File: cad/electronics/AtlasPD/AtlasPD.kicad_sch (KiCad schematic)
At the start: 0 parts

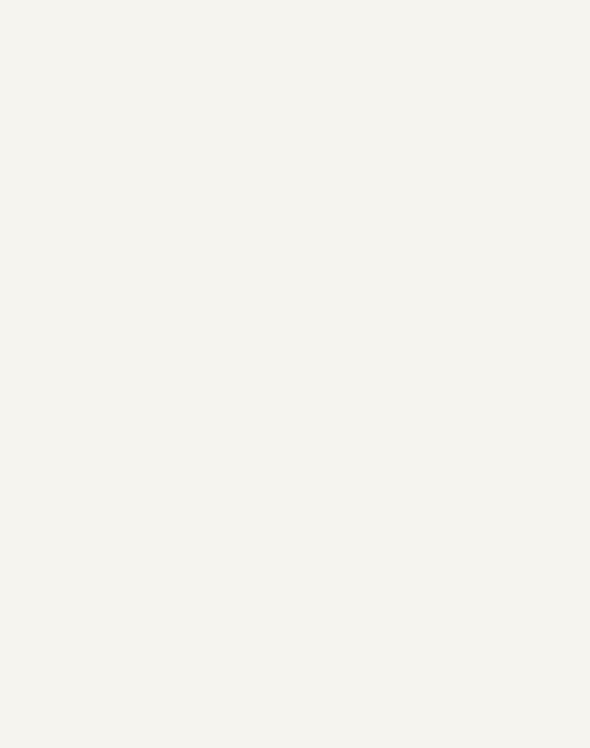
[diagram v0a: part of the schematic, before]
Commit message: Changing MCU design due to chip shortage affecting current design/plans
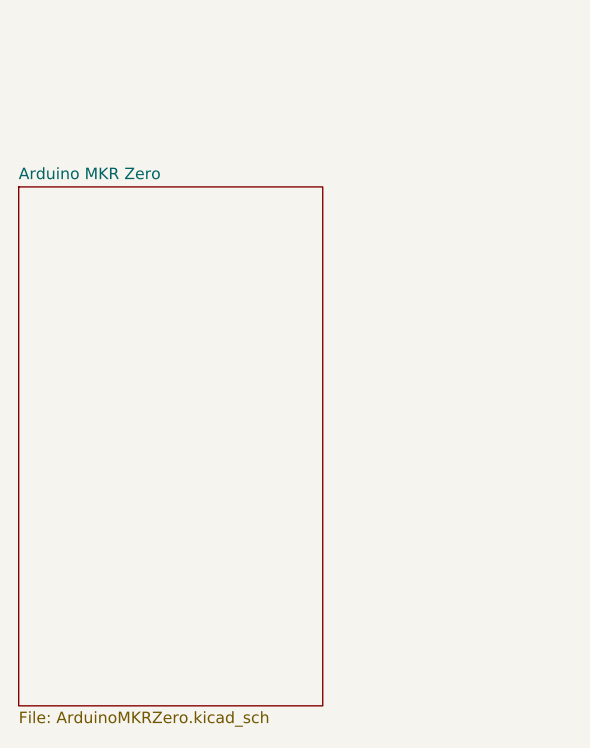
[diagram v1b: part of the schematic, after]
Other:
- added sheet Arduino MKR Zero (ArduinoMKRZero.kicad_sch)
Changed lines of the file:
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@@
+    )
+  )
+  (sheet (at 77.216 83.312) (size 33.782 57.658) (fields_autoplaced)
+    (stroke (width 0.1524) (type solid) (color 0 0 0 0))
+    (fill (color 0 0 0 0.0000))
+    (property "Sheet name" "Arduino MKR Zero" (id 0) (at 77.216 82.6004 0)
+      (effects (font (size 1.27 1.27)) (justify left bottom))
+    )
+    (property "Sheet file" "ArduinoMKRZero.kicad_sch" (id 1) (at 77.216 141.5546 0)
+      (effects (font (size 1.27 1.27)) (justify left top))
     )
   )
@@
     (path "/00000000-0000-0000-0000-000060a23887" (page "3"))
     (path "/00000000-0000-0000-0000-000060a2e58b" (page "4"))
+    (path "/db00ed9d-5cbd-42e1-a367-f32e41a8348a" (page "5"))
   )
   (symbol_instances
@@
       (reference "U402") (unit 1) (value "DS2777") (footprint "SamacSys_Parts:DS2777G+")
     )
+    (path "/db00ed9d-5cbd-42e1-a367-f32e41a8348a/5d6bfee8-45c2-4914-ad4b-302ee1d5f60e"
+      (reference "U500") (unit 1) (value "Arduino_MKR_Zero") (footprint "SamacSys_Parts:Arduino MKR Zero")
+    )
     (path "/00000000-0000-0000-0000-000060a2e58b/00000000-0000-0000-0000-0000616f5a36"

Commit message: Layout updates for MKR
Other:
- sheet Arduino MKR Zero ports: added EN, IN_1, IN_2, IN_3, IN_4, S1, S2, S3, S4; removed none
